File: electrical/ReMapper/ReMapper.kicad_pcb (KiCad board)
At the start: 4 copper layers, 32 x 55 mm, 42 parts, among them J1 ESP_UART0, J2 I2C Display, J3 USB_IN, J4 USB_OUT, J5 Button GND Pad, J9 Button Socket, U1 SPX1117M3-L-3-3/TR, U2 W25Q128JVE, U3 ESP32-S3-WROOM-1-N8R8, U4 RP2040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

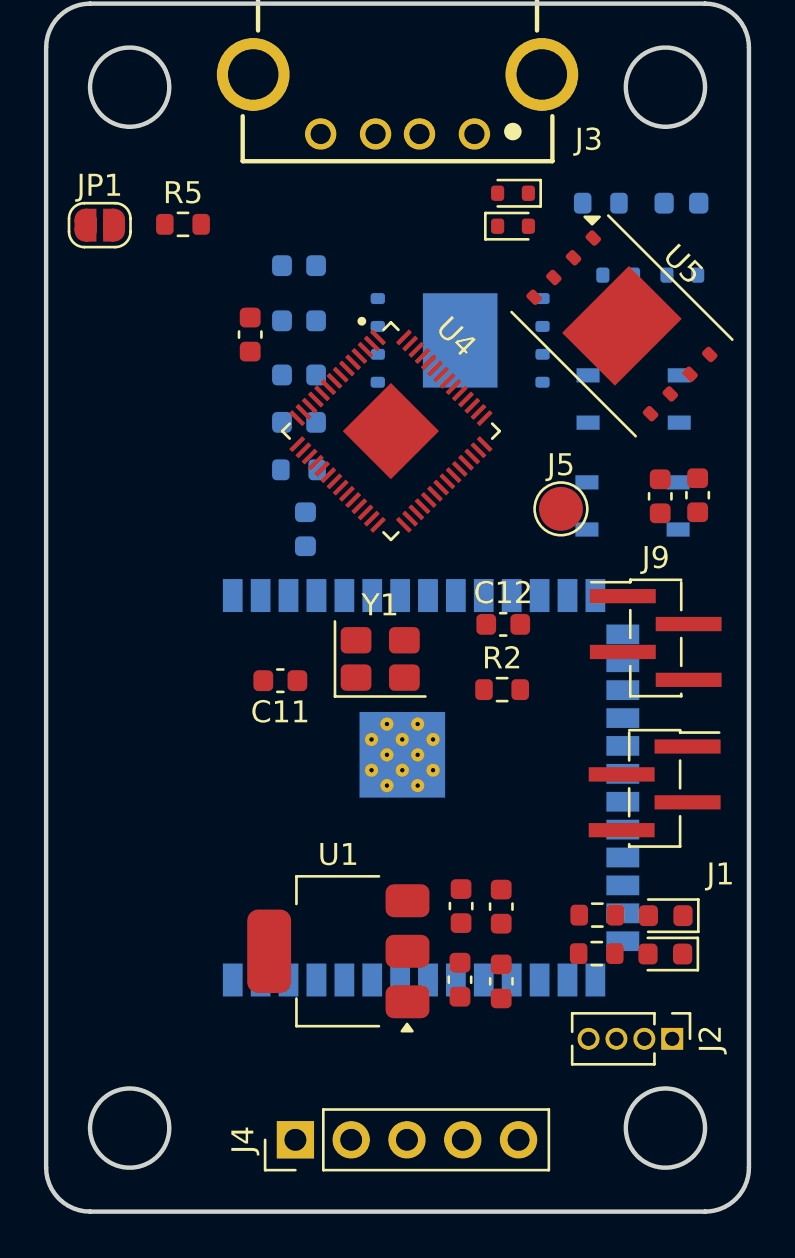
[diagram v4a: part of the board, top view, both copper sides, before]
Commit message: It ssems too small, I need some space for trace highways
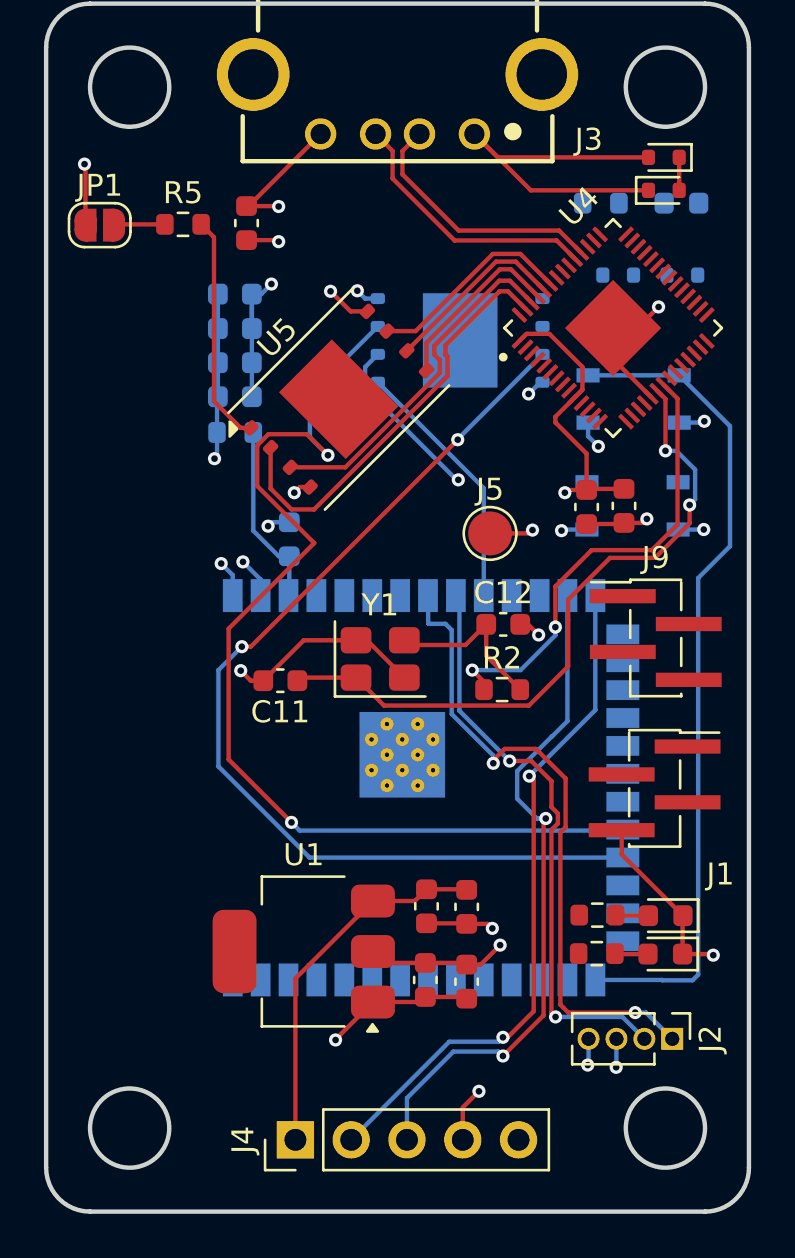
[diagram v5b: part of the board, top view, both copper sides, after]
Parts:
- moved U5 13.3 mm to (179.3, 69.4), turned to 45 degrees
- moved U4 11.2 mm to (191.8, 66.1), turned to 45 degrees
- moved D2 7.55 mm to (194.1, 58.4), turned to 180 degrees
- moved D1 6.87 mm to (194.1, 59.9), turned to 0 degrees
- moved C10 5.08 mm to (175.1, 61.4)
- moved J5 3.41 mm to (186.2, 75.5)
- moved C14 3.39 mm to (192.3, 74.2)
- moved C13 3.39 mm to (190.6, 74.3)
- moved R1 3.37 mm to (174.6, 70.9)
- moved C6 3.20 mm to (174.6, 64.6)
- moved C9 3.15 mm to (174.6, 69.3)
- moved C8 2.97 mm to (174.6, 67.7)
- moved C5 2.94 mm to (174.6, 66.2)
- moved C1 1.58 mm to (185.1, 95.9)
- moved C3 1.58 mm to (183.3, 92.5)
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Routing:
- net GND: track 0.00 -> 70.4 mm, vias 0 -> 21
- net /QSPI_IO2_esp: track 0.00 -> 47.6 mm, vias 0 -> 2
- net /QSPI_IO3_esp: track 0.00 -> 45.2 mm, vias 0 -> 2
- net /ESP_IO0: track 0.00 -> 37.8 mm
- net /3.3V: track 0.00 -> 34.6 mm, vias 0 -> 8
- net /USB_VIN: track 0.00 -> 34.2 mm
- net /USB_OUT_D-: track 0.00 -> 31.0 mm, vias 0 -> 2
- net /XIN_rp: track 0.00 -> 30.8 mm, vias 0 -> 2
- net /USB_OUT_D+: track 0.00 -> 30.7 mm, vias 0 -> 2
- net /I2C_DATA_DISPLAY: track 0.00 -> 29.6 mm, vias 0 -> 2
- net /I2C_CLK_DISPLAY: track 0.00 -> 26.3 mm, vias 0 -> 2
- net /XOUT_rp: track 0.00 -> 21.2 mm, vias 0 -> 2
- net /QSPI_IO1_rp: track 0.00 -> 19.3 mm
- net /QSPI_IO2_rp: track 0.00 -> 16.0 mm
- net /USB_IN_D+: track 0.00 -> 12.2 mm
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- added copper zone on In2.Cu, net /3.3V
- added copper zone on In1.Cu, net GND

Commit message: way happier with this layout
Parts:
- J2: moved to B.Cu
- LED1, R3: moved to F.Cu
- moved D2 36.1 mm to (204.0, 93.1)
- moved S2 33.5 mm to (208.9, 98.7), turned to 0 degrees
- moved D1 33.1 mm to (204.1, 91.5)
- moved C10 31.9 mm to (206.0, 53.5), turned to 0 degrees
- moved LED1 30.6 mm to (209.1, 87.5), turned to 90 degrees
- moved JP1 30.4 mm to (197.0, 72.0), turned to 90 degrees
- moved C5 30.0 mm to (204.1, 71.8), turned to -90 degrees
- moved R3 29.9 mm to (209.1, 84.5), turned to -90 degrees
- moved C6 28.8 mm to (202.5, 71.8), turned to -90 degrees
- moved R6 28.4 mm to (201.3, 68.1), turned to -90 degrees
- moved C11 27.3 mm to (202.8, 74.4)
- moved LED3 27.1 mm to (199.8, 68.1), turned to 90 degrees
- moved Y1 26.5 mm to (206.5, 73.4)
- moved R2 26.0 mm to (209.5, 70.2), turned to -90 degrees
- moved R5 25.7 mm to (197.0, 68.5), turned to 90 degrees
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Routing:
- net GND: track 70.4 -> 0.00 mm, vias 21 -> 0
- net /QSPI_IO2_esp: track 47.6 -> 0.00 mm, vias 2 -> 0
- net /QSPI_IO3_esp: track 45.2 -> 0.00 mm, vias 2 -> 0
- net /ESP_IO0: track 37.8 -> 0.00 mm
- net /3.3V: track 34.6 -> 0.00 mm, vias 8 -> 0
- net /USB_VIN: track 34.2 -> 0.00 mm
- net /USB_OUT_D-: track 31.0 -> 0.00 mm, vias 2 -> 0
- net /XIN_rp: track 30.8 -> 0.00 mm, vias 2 -> 0
- net /USB_OUT_D+: track 30.7 -> 0.00 mm, vias 2 -> 0
- net /I2C_DATA_DISPLAY: track 29.6 -> 0.00 mm, vias 2 -> 0
- net /I2C_CLK_DISPLAY: track 26.3 -> 0.00 mm, vias 2 -> 0
- net /XOUT_rp: track 21.2 -> 0.00 mm, vias 2 -> 0
- net /QSPI_IO1_rp: track 19.3 -> 0.00 mm
- net /QSPI_IO2_rp: track 16.0 -> 0.00 mm
- net /USB_IN_D+: track 12.2 -> 0.00 mm
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- removed copper zone on In2.Cu, net /3.3V
- removed copper zone on In1.Cu, net GND
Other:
- board size 32 x 55 mm -> 35 x 65 mm

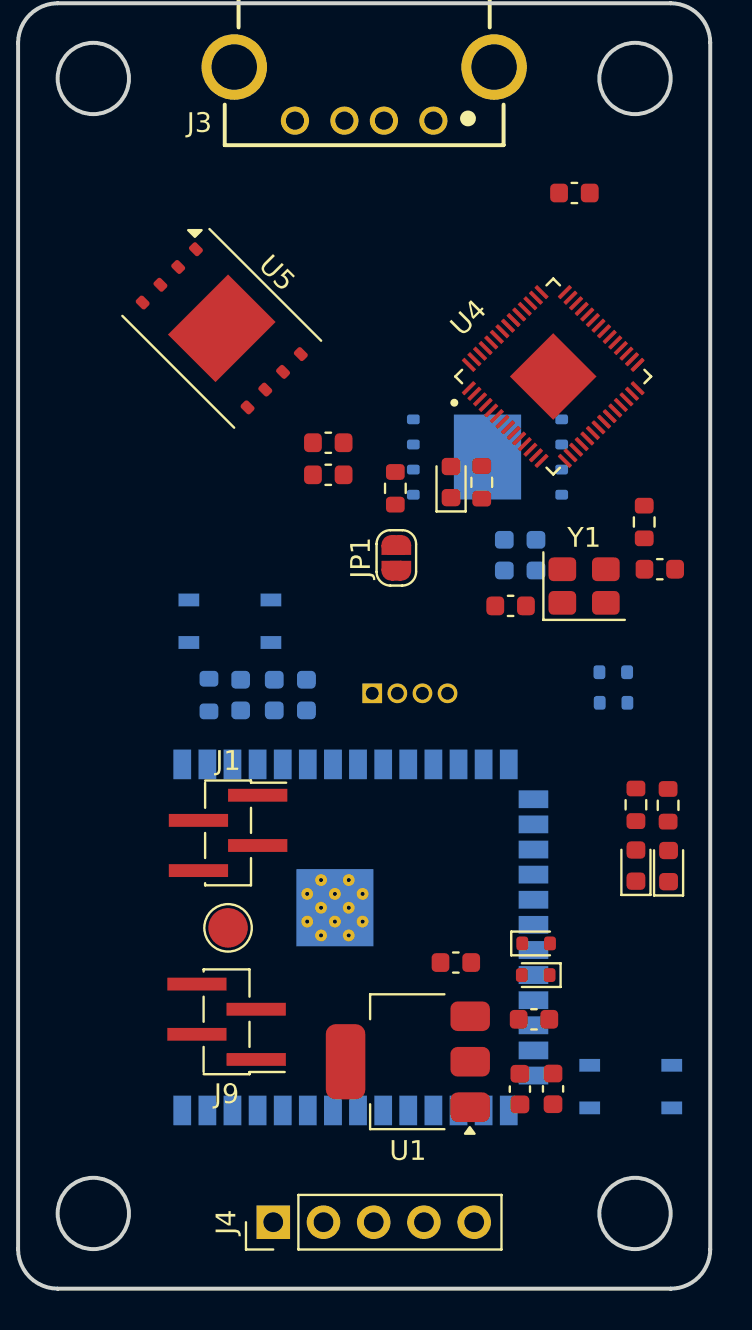
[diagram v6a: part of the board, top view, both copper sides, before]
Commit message: only warnings left on DRC
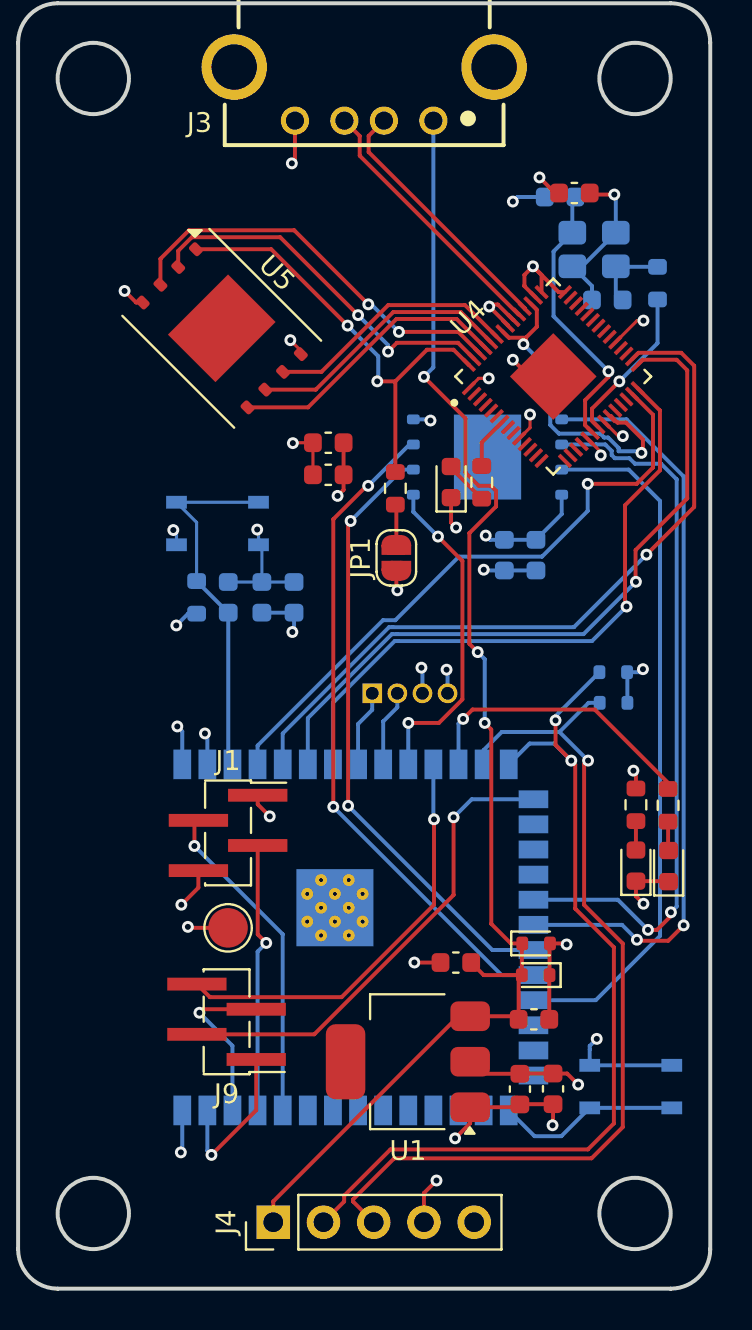
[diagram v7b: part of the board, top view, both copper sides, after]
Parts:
- C11, C12, R2, Y1: moved to B.Cu
- moved C11 20.8 mm to (205.3, 53.7)
- moved Y1 17.0 mm to (207.0, 56.4)
- moved C12 13.9 mm to (207.7, 58.9), turned to 180 degrees
- moved R2 12.1 mm to (210.2, 58.1), turned to 90 degrees
- moved C2 4.98 mm to (188.5, 74.0)
- moved R1 4.98 mm to (186.9, 74.0)
- moved S1 4.98 mm to (188.0, 70.2)
- moved C8 4.98 mm to (191.8, 74.0)
- moved C9 4.98 mm to (190.2, 74.0)
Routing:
- net /USB_VIN: track 0.00 -> 69.8 mm, vias 0 -> 3
- net GND: track 0.00 -> 68.9 mm, vias 0 -> 26
- net /USB_OUT_D-: track 0.00 -> 45.8 mm, vias 0 -> 2
- net /USB_OUT_D+: track 0.00 -> 45.8 mm, vias 0 -> 1
- net /3.3V: track 0.00 -> 40.1 mm, vias 0 -> 17
- net /QSPI_IO0_esp: track 0.00 -> 38.3 mm, vias 0 -> 2
- net /SPI2_MISO: track 0.00 -> 37.8 mm, vias 0 -> 1
- net /QSPI_CLK_esp: track 0.00 -> 36.7 mm, vias 0 -> 2
- net /SPI2_CLK: track 0.00 -> 36.4 mm, vias 0 -> 1
- net /QSPI_IO3_esp: track 0.00 -> 35.4 mm
- net /QSPI_IO2_esp: track 0.00 -> 33.8 mm, vias 0 -> 2
- net /SPI2_CS: track 0.00 -> 32.2 mm, vias 0 -> 1
- net /SPI2_MOSI: track 0.00 -> 31.7 mm, vias 0 -> 1
- net /QSPI_IO1_esp: track 0.00 -> 31.1 mm, vias 0 -> 2
- net /ESP_BUTTON_3: track 0.00 -> 24.2 mm, vias 0 -> 1
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- added copper zone on In2.Cu, net /3.3V
- added copper zone on In1.Cu, net GND

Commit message: drc passed, added silkscreen
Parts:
- added G***: LOGO, LOGO, F.Cu at (184.4, 73.8)
- moved J3 1.51 mm to (195.9, 45.3)
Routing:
- net GND: track 68.9 -> 71.6 mm
- net /USB_VIN: track 69.8 -> 68.6 mm
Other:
- board text added: "3.3V"
- board text added: "33V"
- board text added: "33V LED"
- board text added: "B1"
- board text added: "B2"
- board text added: "B3"
- board text added: "CLK"
- board text added: "D+"
- board text added: "D-"
- board text added: "DATA"
- board text added: "ESP ENB"
- board text added: "ESP LED"
- board text added: "ESP UART"
- board text added: "ESP prog"
- board text added: "GND"
- board text added: "PROG"
- board text added: "RX"
- board text added: "ReMapper Rev4 CedarHacks.com"
- board text added: "TX"
- board text added: "VIN"
